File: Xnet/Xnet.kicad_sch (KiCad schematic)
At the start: 8 parts, among them J2 RJ12, J3 RJ12, U3 MAX485E

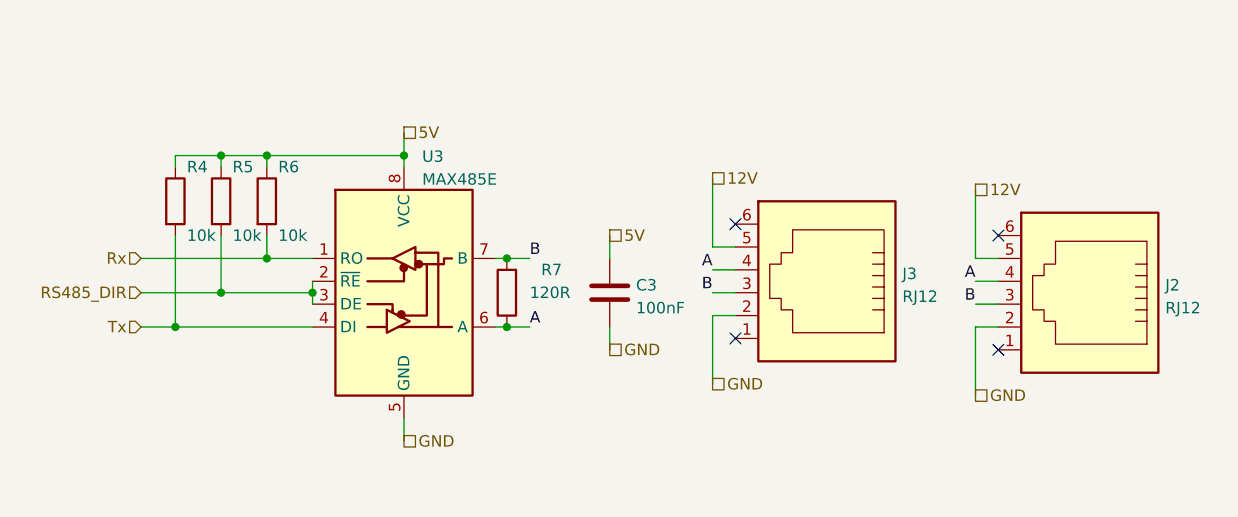
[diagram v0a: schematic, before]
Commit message: moved some schematic scheets to their own folders and routed a board with it. This allow for re-use of PCB parts.
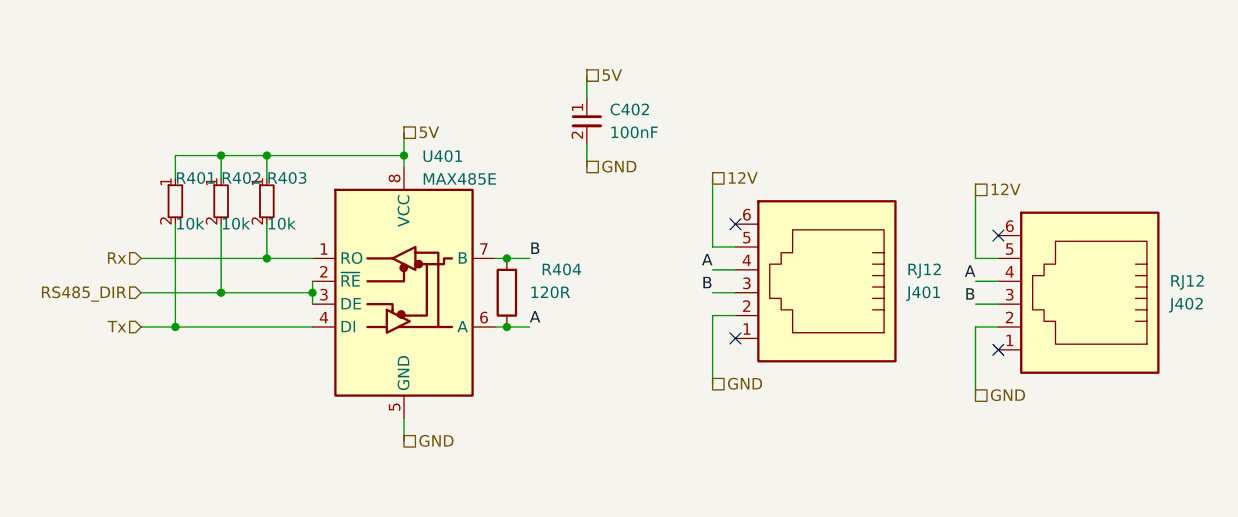
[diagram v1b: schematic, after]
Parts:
- removed C3: 100nF, Capacitor_SMD:C_0603_1608Metric, symbol Device:C
- removed J2, J3: RJ12, Connector_RJ:RJ12_Amphenol_54601, symbol Connector:RJ12
- removed R4, R5, R6: 10k, Resistor_SMD:R_0402_1005Metric, symbol Device:R
- added C402: 100nF, Capacitor_SMD:C_0402_1005Metric, symbol capacitor_miscellaneous:C_0402_100nF
- added J401, J402: RJ12, custom_kicad_lib_sk:RJ12, symbol custom_kicad_lib_sk:RJ12
- added R401, R402, R403: 10k, custom_kicad_lib_sk:R_0603_smalltext, symbol resistors_0603:R_10k_0603
- renumbered R7 to R404, U3 to U401
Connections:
- net 12V: now also J401.5, J402.5
- net 5V: now also C402.1, R401.1, R402.1, R403.1
- net A: now also J401.4, J402.4
- net B: now also J401.3, J402.3
- net GND: now also C402.2, J401.2, J402.2
- net RS485_DIR: now also R402.2
- net Rx: now also R403.2
- net Tx: now also R401.2

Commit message: added 12V boost converter (300mA max!)
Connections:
- net 12V renamed +12V
- net 5V renamed +5V
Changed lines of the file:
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@@
     (effects (font (size 1.27 1.27)) (justify right))
-  )
-  (hierarchical_label "GND" (shape passive) (at 105.41 97.79 0) (fields_autoplaced)
-    (effects (font (size 1.27 1.27)) (justify left))
-  )
-  (hierarchical_label "GND" (shape passive) (at 134.62 99.06 0) (fields_autoplaced)
-    (effects (font (size 1.27 1.27)) (justify left))
-  )
-  (hierarchical_label "GND" (shape passive) (at 91.44 73.66 0) (fields_autoplaced)
-    (effects (font (size 1.27 1.27)) (justify left))
   )
   (hierarchical_label "Rx" (shape input) (at 41.91 83.82 180) (fields_autoplaced)
     (effects (font (size 1.27 1.27)) (justify right))
   )
-  (hierarchical_label "12V" (shape passive) (at 134.62 76.2 0) (fields_autoplaced)
-    (effects (font (size 1.27 1.27)) (justify left))
-  )
-  (hierarchical_label "GND" (shape passive) (at 71.12 104.14 0) (fields_autoplaced)
-    (effects (font (size 1.27 1.27)) (justify left))
-  )
-  (hierarchical_label "5V" (shape passive) (at 91.44 63.5 0) (fields_autoplaced)
-    (effects (font (size 1.27 1.27)) (justify left))
-  )
   (hierarchical_label "Tx" (shape input) (at 41.91 91.44 180) (fields_autoplaced)
     (effects (font (size 1.27 1.27)) (justify right))
-  )
-  (hierarchical_label "12V" (shape passive) (at 105.41 74.93 0) (fields_autoplaced)
-    (effects (font (size 1.27 1.27)) (justify left))
-  )
-  (hierarchical_label "5V" (shape passive) (at 71.12 69.85 0) (fields_autoplaced)
-    (effects (font (size 1.27 1.27)) (justify left))
   )
   (symbol (lib_id "Device:R") (at 82.55 87.63 180) (unit 1)
@@
     )
   )
+  (symbol (lib_id "power:GND") (at 134.62 99.06 0) (unit 1)
+    (in_bom yes) (on_board yes) (dnp no) (fields_autoplaced)
+    (property "Reference" "#PWR0107" (at 134.62 105.41 0)
+      (effects (font (size 1.27 1.27)) hide)
+    )
+    (property "Value" "GND" (at 134.62 104.14 0)
+      (effects (font (size 1.27 1.27)))
+    )
+    (property "Footprint" "" (at 134.62 99.06 0)
+      (effects (font (size 1.27 1.27)) hide)
+    )
+    (property "Datasheet" "" (at 134.62 99.06 0)
+      (effects (font (size 1.27 1.27)) hide)
+    )
+    (pin "1")
+    (instances
+      (project "Xnet"
+        (path "/df188e2b-6a25-44a4-a83d-a1c4efcf9e12"
+          (reference "#PWR0107") (unit 1)
+        )
+      )
+    )
+  )
   (symbol (lib_id "resistors_0603:R_10k_0603") (at 50.8 77.47 0) (unit 1)
     (in_bom yes) (on_board yes) (dnp no)
@@
         (path "/df188e2b-6a25-44a4-a83d-a1c4efcf9e12"
           (reference "R403") (unit 1)
+        )
+      )
+    )
+  )
+  (symbol (lib_id "power:+12V") (at 134.62 76.2 0) (unit 1)
+    (in_bom yes) (on_board yes) (dnp no) (fields_autoplaced)
+    (property "Reference" "#PWR0101" (at 134.62 80.01 0)
+      (effects (font (size 1.27 1.27)) hide)
+    )
+    (property "Value" "+12V" (at 134.62 71.12 0)
+      (effects (font (size 1.27 1.27)))
+    )
+    (property "Footprint" "" (at 134.62 76.2 0)
+      (effects (font (size 1.27 1.27)) hide)
+    )
+    (property "Datasheet" "" (at 134.62 76.2 0)
+      (effects (font (size 1.27 1.27)) hide)
+    )
+    (pin "1")
+    (instances
+      (project "Xnet"
+        (path "/df188e2b-6a25-44a4-a83d-a1c4efcf9e12"
+          (reference "#PWR0101") (unit 1)
+        )
+      )
+    )
+  )
+  (symbol (lib_id "power:GND") (at 91.44 73.66 0) (unit 1)
+    (in_bom yes) (on_board yes) (dnp no) (fields_autoplaced)
+    (property "Reference" "#PWR0108" (at 91.44 80.01 0)
+      (effects (font (size 1.27 1.27)) hide)
+    )
+    (property "Value" "GND" (at 91.44 78.74 0)
+      (effects (font (size 1.27 1.27)))
+    )
+    (property "Footprint" "" (at 91.44 73.66 0)
+      (effects (font (size 1.27 1.27)) hide)
+    )
+    (property "Datasheet" "" (at 91.44 73.66 0)
+      (effects (font (size 1.27 1.27)) hide)
+    )
+    (pin "1")
+    (instances
+      (project "Xnet"
+        (path "/df188e2b-6a25-44a4-a83d-a1c4efcf9e12"
+          (reference "#PWR0108") (unit 1)
         )
       )
@@
     )
   )
+  (symbol (lib_id "power:+5V") (at 91.44 63.5 0) (unit 1)
+    (in_bom yes) (on_board yes) (dnp no) (fields_autoplaced)
+    (property "Reference" "#PWR0104" (at 91.44 67.31 0)
+      (effects (font (size 1.27 1.27)) hide)
+    )
+    (property "Value" "+5V" (at 91.44 58.42 0)
+      (effects (font (size 1.27 1.27)))
+    )
+    (property "Footprint" "" (at 91.44 63.5 0)
+      (effects (font (size 1.27 1.27)) hide)
+    )
+    (property "Datasheet" "" (at 91.44 63.5 0)
+      (effects (font (size 1.27 1.27)) hide)
+    )
+    (pin "1")
+    (instances
+      (project "Xnet"
+        (path "/df188e2b-6a25-44a4-a83d-a1c4efcf9e12"
+          (reference "#PWR0104") (unit 1)
+        )
+      )
+    )
+  )
+  (symbol (lib_id "power:+12V") (at 105.41 74.93 0) (unit 1)
+    (in_bom yes) (on_board yes) (dnp no) (fields_autoplaced)
+    (property "Reference" "#PWR0102" (at 105.41 78.74 0)
+      (effects (font (size 1.27 1.27)) hide)
+    )
+    (property "Value" "+12V" (at 105.41 69.85 0)
+      (effects (font (size 1.27 1.27)))
+    )
+    (property "Footprint" "" (at 105.41 74.93 0)
+      (effects (font (size 1.27 1.27)) hide)
+    )
+    (property "Datasheet" "" (at 105.41 74.93 0)
+      (effects (font (size 1.27 1.27)) hide)
+    )
+    (pin "1")
+    (instances
+      (project "Xnet"
+        (path "/df188e2b-6a25-44a4-a83d-a1c4efcf9e12"
+          (reference "#PWR0102") (unit 1)
+        )
+      )
+    )
+  )
+  (symbol (lib_id "power:GND") (at 105.41 97.79 0) (unit 1)
+    (in_bom yes) (on_board yes) (dnp no) (fields_autoplaced)
+    (property "Reference" "#PWR0106" (at 105.41 104.14 0)
+      (effects (font (size 1.27 1.27)) hide)
+    )
+    (property "Value" "GND" (at 105.41 102.87 0)
+      (effects (font (size 1.27 1.27)))
+    )
+    (property "Footprint" "" (at 105.41 97.79 0)
+      (effects (font (size 1.27 1.27)) hide)
+    )
+    (property "Datasheet" "" (at 105.41 97.79 0)
+      (effects (font (size 1.27 1.27)) hide)
+    )
+    (pin "1")
+    (instances
+      (project "Xnet"
+        (path "/df188e2b-6a25-44a4-a83d-a1c4efcf9e12"
+          (reference "#PWR0106") (unit 1)
+        )
+      )
+    )
+  )
   (symbol (lib_id "resistors_0603:R_10k_0603") (at 45.72 77.47 0) (unit 1)
     (in_bom yes) (on_board yes) (dnp no)
@@
         )
       )
+    )
+  )
+  (symbol (lib_id "power:GND") (at 71.12 104.14 0) (unit 1)
+    (in_bom yes) (on_board yes) (dnp no) (fields_autoplaced)
+    (property "Reference" "#PWR0105" (at 71.12 110.49 0)
+      (effects (font (size 1.27 1.27)) hide)
+    )
+    (property "Value" "GND" (at 71.12 109.22 0)
+      (effects (font (size 1.27 1.27)))
+    )
+    (property "Footprint" "" (at 71.12 104.14 0)
+      (effects (font (size 1.27 1.27)) hide)
+    )
+    (property "Datasheet" "" (at 71.12 104.14 0)
+      (effects (font (size 1.27 1.27)) hide)
+    )
+    (pin "1")
+    (instances
+      (project "Xnet"
+        (path "/df188e2b-6a25-44a4-a83d-a1c4efcf9e12"
+          (reference "#PWR0105") (unit 1)
+        )
+      )
+    )
+  )
+  (symbol (lib_id "power:+5V") (at 71.12 69.85 0) (unit 1)
+    (in_bom yes) (on_board yes) (dnp no) (fields_autoplaced)
+    (property "Reference" "#PWR0103" (at 71.12 73.66 0)
+      (effects (font (size 1.27 1.27)) hide)
+    )
+    (property "Value" "+5V" (at 71.12 64.77 0)
+      (effects (font (size 1.27 1.27)))
+    )
+    (property "Footprint" "" (at 71.12 69.85 0)
+      (effects (font (size 1.27 1.27)) hide)
+    )
+    (property "Datasheet" "" (at 71.12 69.85 0)
+      (effects (font (size 1.27 1.27)) hide)
+    )
+    (pin "1")
+    (instances
+      (project "Xnet"
+        (path "/df188e2b-6a25-44a4-a83d-a1c4efcf9e12"
+          (reference "#PWR0103") (unit 1)
+        )
+      )
